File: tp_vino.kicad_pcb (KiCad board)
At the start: 2 copper layers, 96 parts, among them J1 TB_1X2, J10 PotO.Out, J2 TB_1X2, J3 TB_1X2, J4 TB_1X2, J5 TB_1X2, J6 V.RegOut, J7 Temp.Out, J8 C.RegOut, J9 PotTOut, P1 CONN_02X02, P10 3.3_GND_5V, P11 CONN_01X06, P12 CONN_01X06, P2 USB_OTG, P3 CONN_01X03, P4 Pot2_Out, P5 C.reg.in, P6 V_regOut, P7 Temp_Out, P8 C_RegOut, P9 PotO_Out, Q1 BC849, Q2 BC849, Q3 BC849, Q4 BC849, Q5 BC849, SW1 TEC_1, SW2 TEC_1, SW3 TEC_1, SW4 TEC_1, U1 ST3232E, U2 LM2576HVS-5, U3 NCP1117ST33T3G, U4 LM317_SOT223, U5 LM317_SOT223, U6 LM35-LP, U7 SIM800L

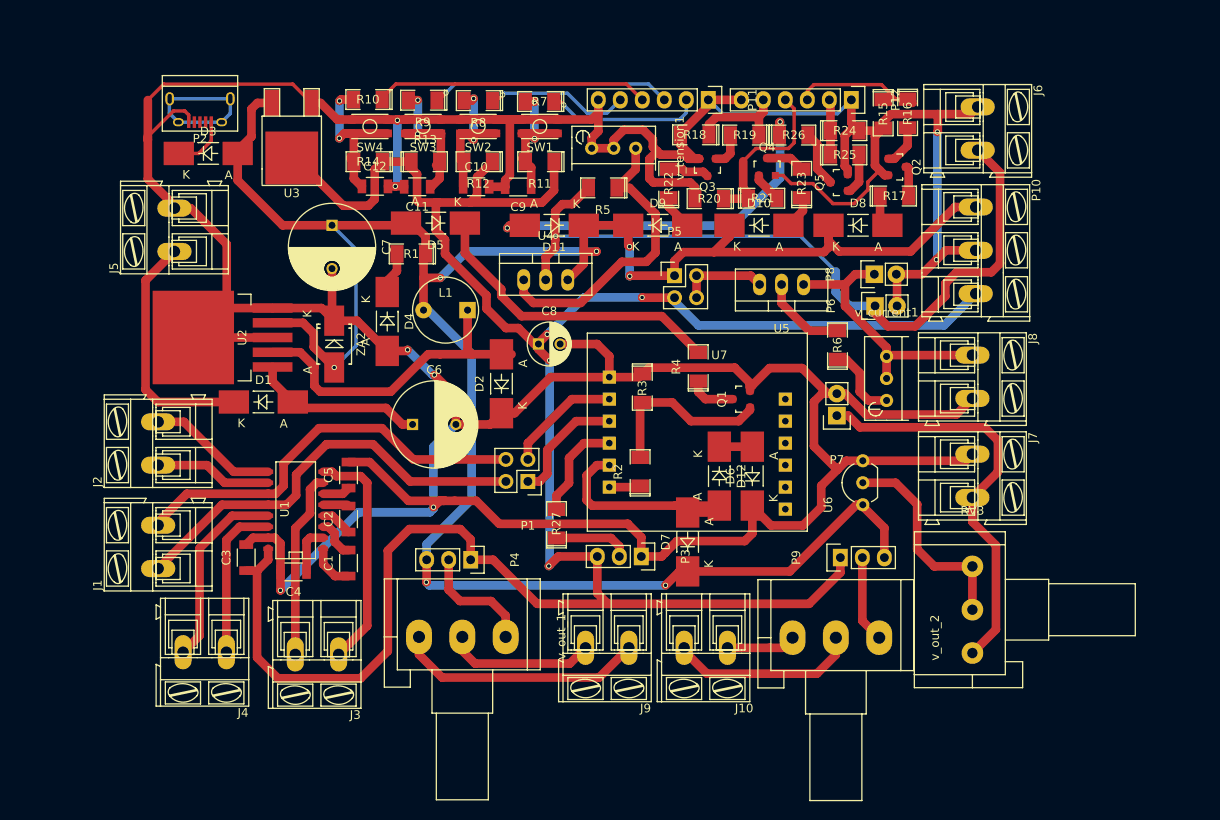
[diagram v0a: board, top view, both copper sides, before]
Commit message: Agrego los graficos para el esquematico en 3d.
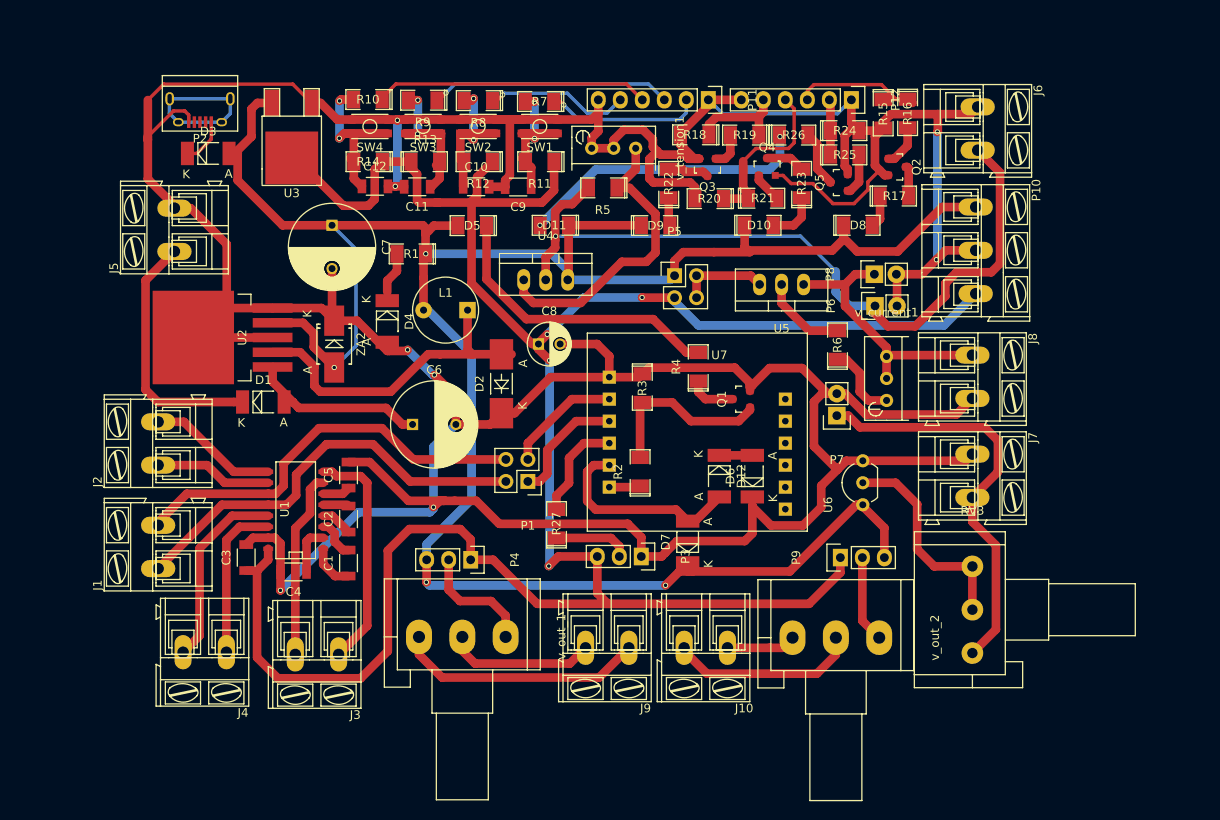
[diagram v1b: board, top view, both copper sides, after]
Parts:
- D1, D12, D3, D4, D6, D7: footprint Diodes_SMD:MELF_Handsoldering -> Diodes_SMD:MELF_Standard
- D10, D11, D5, D8, D9: footprint Diodes_SMD:MELF_Handsoldering -> SMD_Packages:SMD-1206_Pol
- J1: value TB_1X2 -> TxRx_TTL1
- J2: value TB_1X2 -> TxRx_TTL2
- J3: value TB_1X2 -> TxRx232Out2
- J4: value TB_1X2 -> TxRx232Out1
- J5: value TB_1X2 -> Vin
- P1: value CONN_02X02 -> JmpSim
- P10: value 3.3_GND_5V -> 3.3v_GNF_5v
- P11: value CONN_01X06 -> SwPins
- P12: value CONN_01X06 -> PinLeds
- P3: value CONN_01X03 -> UartSim
- moved D5 4.25 mm to (145.0, 77.3)
- moved D9 0.24 mm to (166.1, 77.3)
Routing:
- net Net-(D11-Pad2): track 44.1 -> 33.7 mm
- net +5V: track 265.3 -> 272.8 mm, vias 7 -> 6
- net GND: track 537.0 -> 539.3 mm
- net Net-(D10-Pad2): track 3.87 -> 5.91 mm
- net +3.3V: track 271.8 -> 269.9 mm
- net Net-(D12-Pad2): track 25.5 -> 23.9 mm
- net Net-(D5-Pad1): track 35.6 -> 34.1 mm
- net Net-(D3-Pad1): track 6.50 -> 5.39 mm
- net Net-(D1-Pad1): track 28.1 -> 29.1 mm
- net Net-(D4-Pad1): track 4.86 -> 5.86 mm
- net Net-(C6-Pad1): track 19.9 -> 20.9 mm
- net Net-(D9-Pad2): track 4.06 -> 3.33 mm
- net Net-(D12-Pad1): track 3.81 -> 4.36 mm

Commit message: Add digikey code and comment schematic.
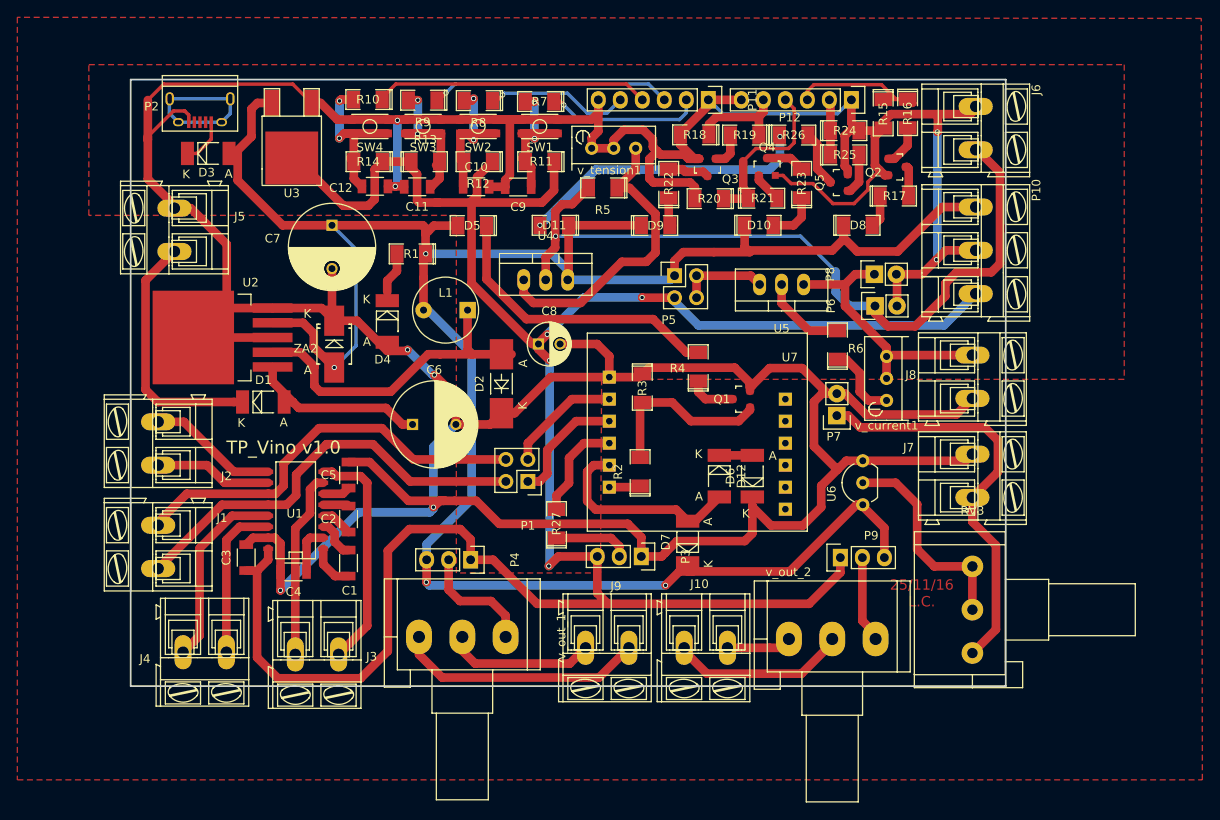
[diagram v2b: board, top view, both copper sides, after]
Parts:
- moved v_out_2 0.45 mm to (191.5, 125.0)
- moved J6 0.23 mm to (203.1, 63.5)
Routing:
- net Net-(J10-Pad2): track 21.8 -> 20.8 mm
- added copper zone on F.Cu, net +3.3V
- added copper zone on F.Cu, net +5V
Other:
- board outline added: 101 x 70 mm
- board text added: "25/11/16 L.C."
- board text added: "TP_Vino v1.0"

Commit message: Actualizo las revisiones y documentaciones faltante. Algunas correcciones realizadas, faltan algunas mas que vere de hacerlas.
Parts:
- moved D10 4.99 mm to (183.0, 78.0), turned to 90 degrees
- turned D5 to 0 degrees
- turned R16 to 90 degrees
- turned R25 to 180 degrees
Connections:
- D5 pad 1: Net-(D5-Pad1) -> +5V
- D5 pad 2: +5V -> Net-(D5-Pad2)
- R16 pad 1: Net-(P12-Pad3) -> Net-(Q2-Pad1)
- R16 pad 2: Net-(Q2-Pad1) -> Net-(P12-Pad3)
- R19 pad 1: Net-(P12-Pad5) -> Net-(Q3-Pad1)
- R19 pad 2: Net-(Q3-Pad1) -> Net-(P12-Pad5)
- R21 pad 1: Net-(P12-Pad4) -> Net-(Q4-Pad1)
- R21 pad 2: Net-(Q4-Pad1) -> Net-(P12-Pad4)
- R25 pad 1: Net-(P12-Pad2) -> Net-(Q5-Pad1)
- R25 pad 2: Net-(Q5-Pad1) -> Net-(P12-Pad2)
- R4 pad 2: Net-(D5-Pad1) -> Net-(D5-Pad2)
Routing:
- net Net-(D5-Pad2): track 0.00 -> 34.1 mm
- net Net-(D5-Pad1): track 34.1 -> 0.00 mm
- net Net-(P12-Pad4): track 19.5 -> 23.7 mm, vias 0 -> 2
- net +5V: track 272.8 -> 268.9 mm
- net Net-(D10-Pad2): track 5.91 -> 2.29 mm
- net Net-(P12-Pad5): track 12.4 -> 9.16 mm
- net Net-(Q3-Pad1): track 4.07 -> 6.13 mm
